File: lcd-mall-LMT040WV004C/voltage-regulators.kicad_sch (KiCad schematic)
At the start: 10 parts, among them U1 RS3236-1.8FY5, U3 AP3127B

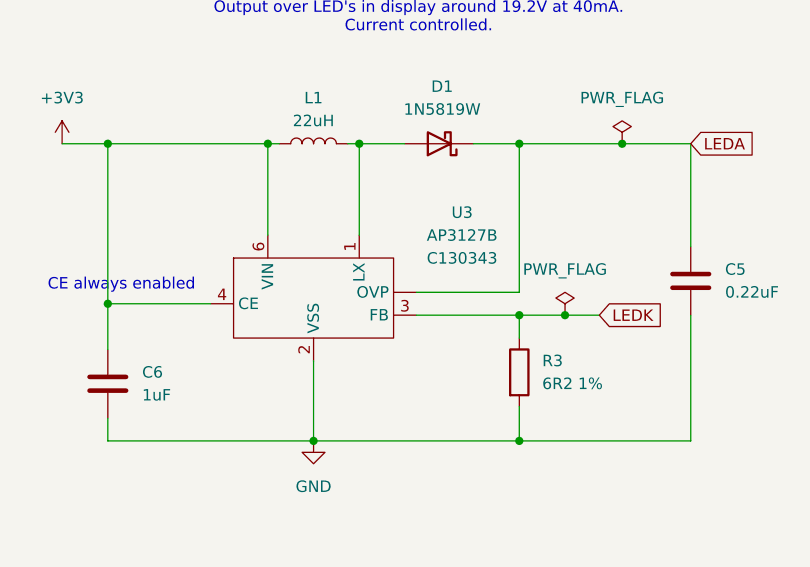
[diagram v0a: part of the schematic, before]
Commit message: Fix names, footprints, and silkscreen of the pcb's
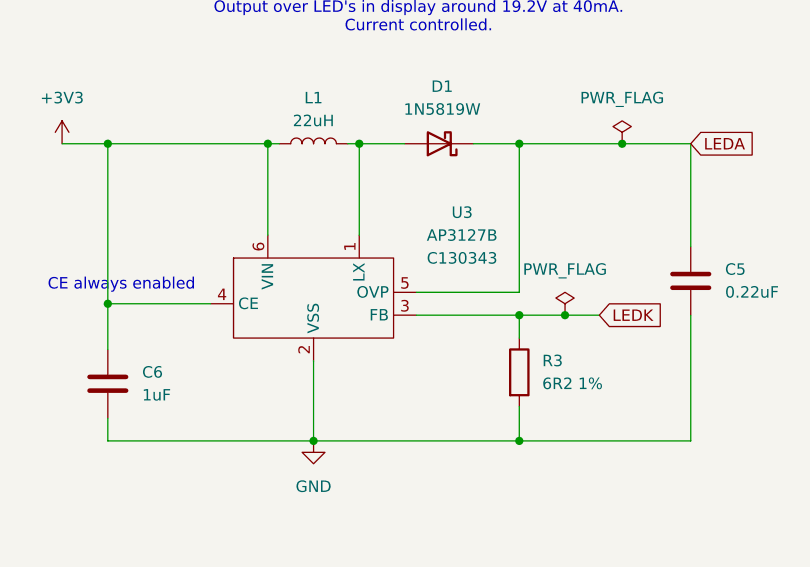
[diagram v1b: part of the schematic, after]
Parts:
- U1: Lcsc C379343 -> C379345
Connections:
- net LEDA: now also U3.5 (OVP); no longer U3. (OVP)
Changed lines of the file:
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@@
 			)
 		)
-		(property "Datasheet" "https://datasheet.lcsc.com/lcsc/1912111437_LGE-1N5819W_C402219.pdf"
+		(property "Datasheet" "~"
 			(at 223.52 33.02 0)
 			(effects
@@
 		(pin "1"
 		)
-		(pin ""
+		(pin "5"
 		)
 		(pin "2"
@@
 			)
 		)
-		(property "Datasheet" "https://www.lcsc.com/datasheet/lcsc_datasheet_2304140030_RALEC-RTT036R34FTP_C166772.pdf"
+		(property "Datasheet" "~"
 			(at 232.41 58.42 0)
 			(effects
@@
 			)
 		)
-		(property "Datasheet" "https://lcsc.com/datasheet/lcsc_datasheet_2304140030_Jiangsu-RUNIC-Tech-RS3236-1-8YF5_C379343.pdf"
+		(property "Datasheet" "https://www.lcsc.com/datasheet/lcsc_datasheet_2304140030_Jiangsu-RUNIC-Tech-RS3236-2-5YF5_C379344.pdf"
 			(at 64.77 45.72 0)
 			(effects
@@
 			)
 		)
-		(property "Lcsc" "C379343"
+		(property "Lcsc" "C379345"
 			(at 64.77 45.72 0)
 			(effects
@@
 			)
 		)
-		(property "Datasheet" "https://www.lcsc.com/datasheet/lcsc_datasheet_2002271926_microgate-MPIT252012-220M-LF_C486445.pdf"
+		(property "Datasheet" "~"
 			(at 209.55 33.02 0)
 			(effects

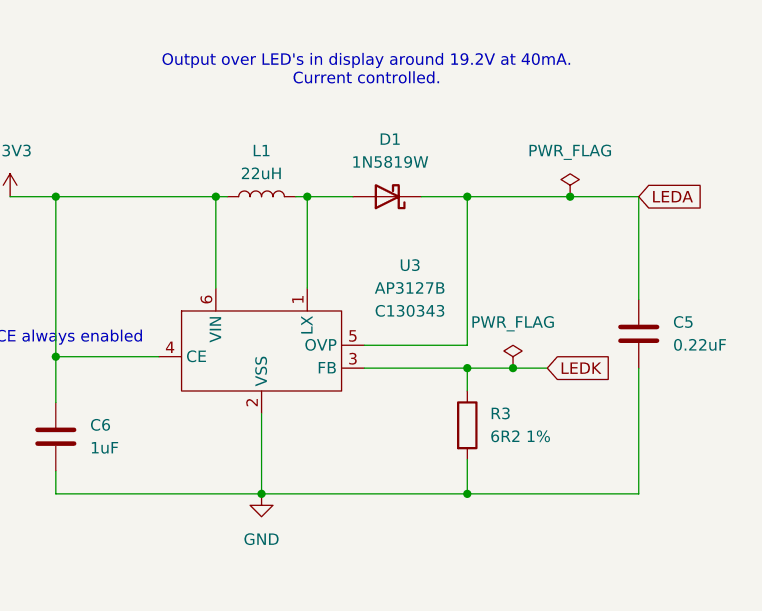
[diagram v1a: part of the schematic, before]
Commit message: Fix parts for board LMT040WM004C
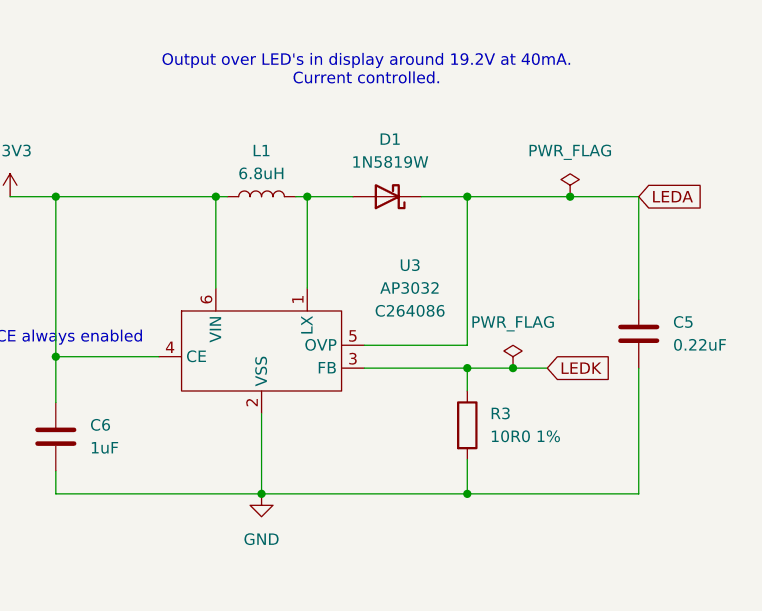
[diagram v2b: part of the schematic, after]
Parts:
- C1, C2, C3, C6: LCSC C5189821 -> C126631
- L1: value 22uH -> 6.8uH; footprint Inductor_SMD:L_Changjiang_FNR252010S -> Inductor_SMD:L_1210_3225Metric; LCSC C486445 -> C394999
- R3: value 6R2 1% -> 10R0 1%; LCSC (none) -> C103222; lcsc C3013206 -> (none)
- U1: LCSC (none) -> C379345; Lcsc C379345 -> (none)
- U3: value AP3127B -> AP3032; LCSC C130343 -> C264086
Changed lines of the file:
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@@
 			)
 		)
-		(property "Value" "AP3127B"
+		(property "Value" "AP3032"
 			(at 226.06 43.2114 0)
 			(effects
@@
 			)
 		)
-		(property "Datasheet" "https://file.remont-aud.net/baza/dc_dc/data/AP3127B.pdf"
+		(property "Datasheet" "https://www.diodes.com/assets/Datasheets/AP3032.pdf"
 			(at 204.47 50.8 0)
 			(effects
@@
 			)
 		)
-		(property "LCSC" "C130343"
+		(property "LCSC" "C264086 "
 			(at 226.06 45.7514 0)
 			(effects
@@
 			)
 		)
-		(property "Value" "6R2 1%"
+		(property "Value" "10R0 1%"
 			(at 234.95 59.6899 0)
 			(effects
@@
 			)
 		)
-		(property "lcsc" "C3013206"
+		(property "LCSC" " C103222 "
 			(at 232.41 58.42 0)
 			(effects
@@
 			)
 		)
-		(property "LCSC" "C5189821"
+		(property "LCSC" "C126631"
 			(at 186.69 59.69 0)
 			(effects
@@
 			)
 		)
-		(property "LCSC" "C5189821"
+		(property "LCSC" "C126631"
 			(at 90.17 46.99 0)
 			(effects
@@
 			)
 		)
-		(property "Lcsc" "C379345"
+		(property "LCSC" "C379345"
 			(at 64.77 45.72 0)
 			(effects
@@
 			)
 		)
-		(property "LCSC" "C5189821"
+		(property "LCSC" "C126631"
 			(at 102.87 41.91 0)
 			(effects
@@
 			)
 		)
-		(property "Value" "22uH"
+		(property "Value" "6.8uH"
 			(at 209.55 30.48 90)
 			(effects
@@
 			)
 		)
-		(property "Footprint" "Inductor_SMD:L_Changjiang_FNR252010S"
+		(property "Footprint" "Inductor_SMD:L_1210_3225Metric"
 			(at 209.55 33.02 0)
 			(effects
@@
 			)
 		)
-		(property "LCSC" "C486445"
+		(property "LCSC" "C394999 "
 			(at 209.55 33.02 90)
 			(effects
@@
 			)
 		)
-		(property "LCSC" "C5189821"
+		(property "LCSC" "C126631"
 			(at 35.56 41.91 0)
 			(effects
